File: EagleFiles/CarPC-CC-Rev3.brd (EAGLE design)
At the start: 75.5 x 80 mm, 72 parts, among them IC10 RN42HID-I/RM, IC2 MCP2515-I_SO, IC3 TJA1050T-CM/118, IC4 INA219AIDR, K1 G3VM-61VR(TR), Q5 16MHz

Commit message: Error in schemic and board: using 5v rail now
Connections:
- net +3V3-ODROID: now also JP-N2.2; no longer JP-N2.1
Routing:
- net +3V3-ODROID: track 3.36 -> 4.34 mm
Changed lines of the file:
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@@
 <drawing>
 <settings>
-<setting alwaysvectorfont="yes"/>
+<setting alwaysvectorfont="no"/>
 <setting verticaltext="up"/>
 </settings>
@@
 </layers>
 <board>
-<fusionsync huburn="a.YnVzaW5lc3M6Z29vZ2xlbWFpbDM5NzQ" projecturn="a.YnVzaW5lc3M6Z29vZ2xlbWFpbDM5NzQjRDIwMjAwMjA2MjYyODQ5OTA2" f3durn="urn:adsk.wipprod:dm.lineage:IggFrhZtQ_a1feRvvqs7Pg" pcbguid="bf3eb248-23ff-493d-88a3-1bcde9847c90" lastpulledtime="" lastsyncedchangeguid="898adb16-6d4d-edbb-685e-6e754855c02e"/>
+<fusionsync huburn="a.YnVzaW5lc3M6Z29vZ2xlbWFpbDM5NzQ" projecturn="a.YnVzaW5lc3M6Z29vZ2xlbWFpbDM5NzQjRDIwMjAwMjA2MjYyODQ5OTA2" f3durn="urn:adsk.wipprod:dm.lineage:80bHzjXET0ueI-K0PMmWLg" pcbguid="6e002f67-a89e-4d15-bfc3-ee707e087338" lastpulledtime="" lastsyncedchangeguid="95f337ff-36ca-174e-4e19-b75f39ef2b8f"/>
 <fusionteam huburn="a.YnVzaW5lc3M6Z29vZ2xlbWFpbDM5NzQ" projecturn="a.YnVzaW5lc3M6Z29vZ2xlbWFpbDM5NzQjRDIwMjAwMjA2MjYyODQ5OTA2" folderUrn="urn:adsk.wipprod:fs.folder:co.GUaS0R9CR3qfWpvkudDapg" urn="urn:adsk.wipprod:dm.lineage:FOIr01fbTJunwoKxbafz_w"  versionUrn="urn:adsk.wipprod:fs.file:vf.FOIr01fbTJunwoKxbafz_w?version=3" camFileUrn="" camFileVersionUrn="" lastpublishedchangeguid="8b2acdfd-6c5f-7b93-8b8e-7720c5fae449"/>
 <plain>
@@
 <signal name="+3V3-ODROID">
 <contactref element="R1" pad="1"/>
-<contactref element="JP-N2" pad="1"/>
-<wire x1="61.75" y1="96.75" x2="64.75" y2="96.75" width="0.5" layer="16"/>
 <wire x1="64.75" y1="96.75" x2="64.77" y2="96.672" width="0.5" layer="16"/>
-<wire x1="61.75" y1="96.75" x2="61.595" y2="96.52" width="0.5" layer="16"/>
+<contactref element="JP-N2" pad="2"/>
+<wire x1="62" y1="94" x2="64.5" y2="96.5" width="0.5" layer="16"/>
+<wire x1="64.5" y1="96.5" x2="64.77" y2="96.672" width="0.5" layer="16"/>
+<wire x1="62" y1="94" x2="61.595" y2="93.98" width="0.5" layer="16"/>
 </signal>
 <signal name="ODROID-PWR-SENS" class="7">

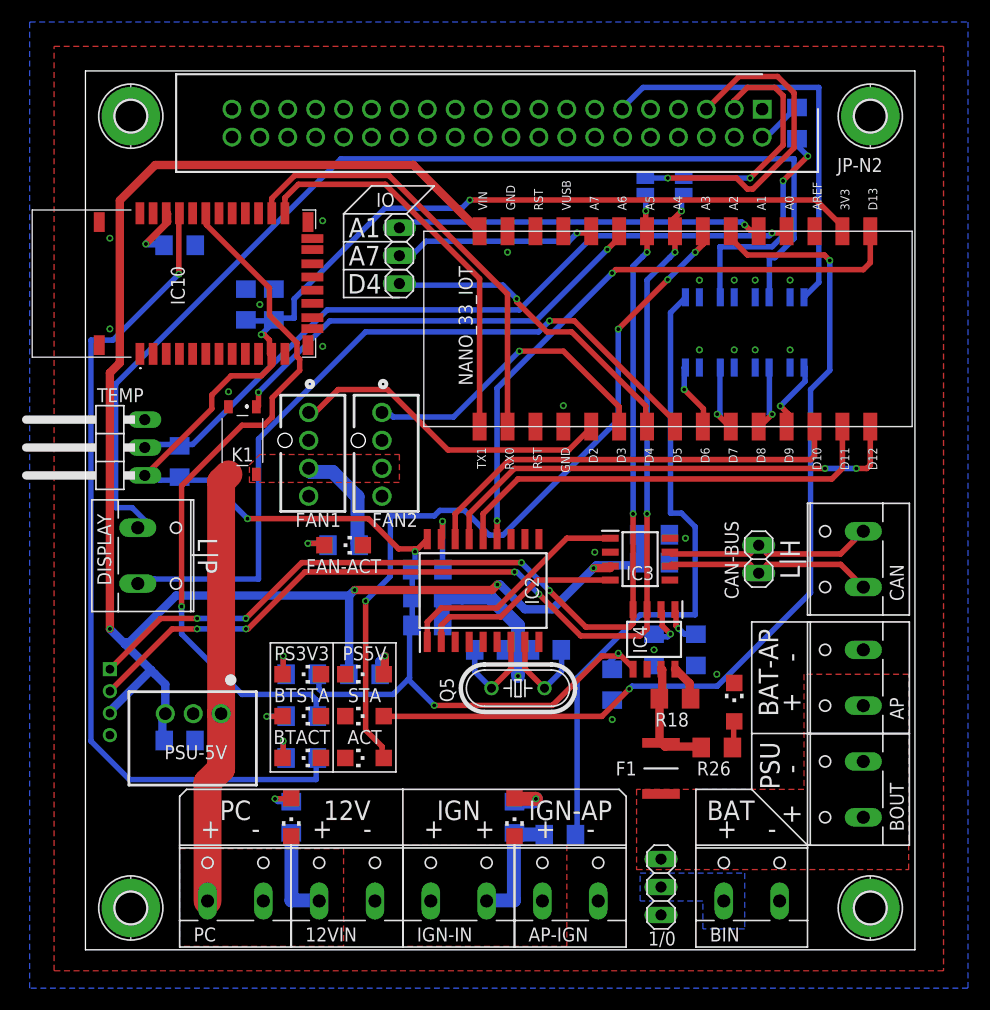
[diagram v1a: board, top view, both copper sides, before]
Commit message: Fan control interferes with display brightness.
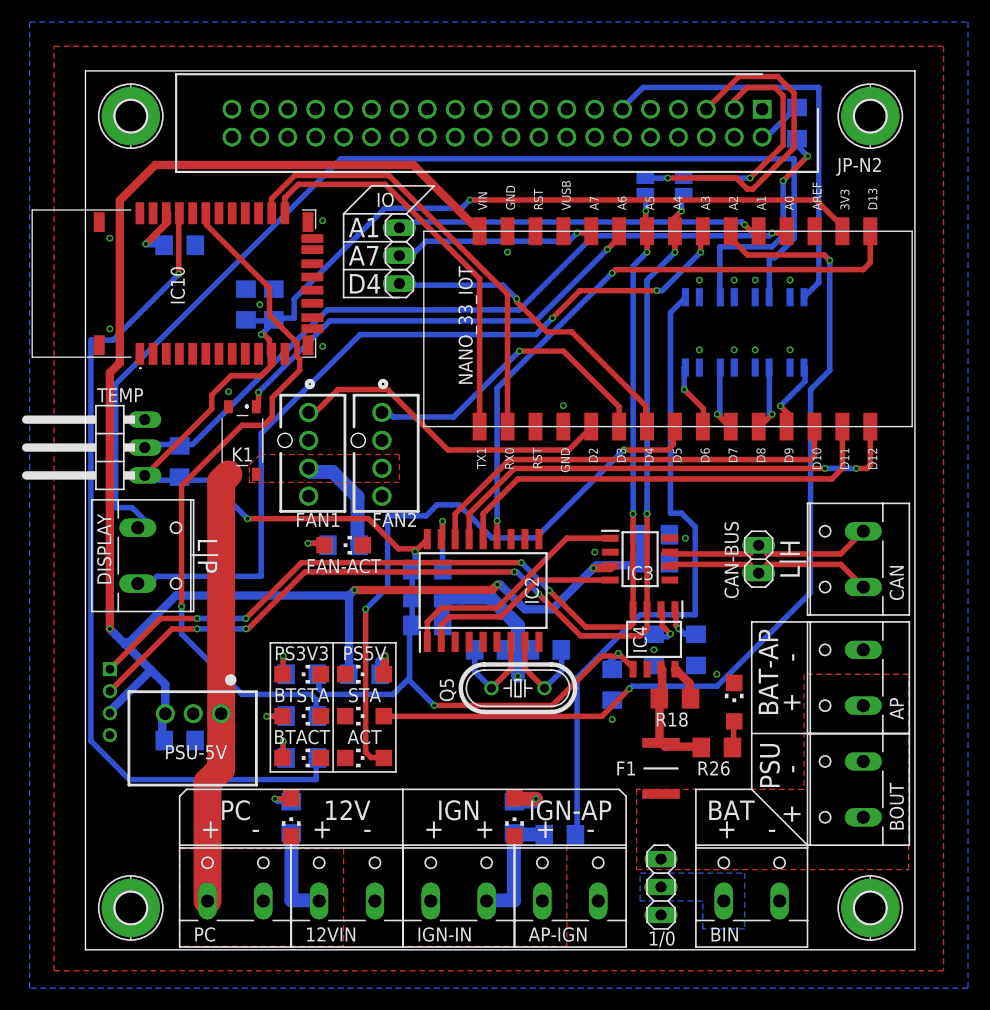
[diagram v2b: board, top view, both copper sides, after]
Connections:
- net DISP-BRIGHT: now also NANO_33_IOT.A3; no longer NANO_33_IOT.D5
- net LED-ACT: now also NANO_33_IOT.D5; no longer NANO_33_IOT.A3
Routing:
- net LED-ACT: track 70.3 -> 57.1 mm, vias 4 -> 2
- net DISP-BRIGHT: track 70.5 -> 73.3 mm, vias 1 -> 3
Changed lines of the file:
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@@
 </signal>
 <signal name="DISP-BRIGHT" class="7">
-<contactref element="NANO_33_IOT" pad="D5"/>
 <contactref element="DISPLAY" pad="2"/>
-<wire x1="53.5" y1="68.25" x2="53.5" y2="67.75" width="0.5" layer="1"/>
-<wire x1="44.5" y1="77.25" x2="53.5" y2="68.25" width="0.5" layer="1"/>
-<wire x1="42.25" y1="77.25" x2="44.5" y2="77.25" width="0.5" layer="1"/>
-<wire x1="41.25" y1="76.25" x2="42.25" y2="77.25" width="0.5" layer="16"/>
-<wire x1="25.5" y1="76.25" x2="41.25" y2="76.25" width="0.5" layer="16"/>
-<wire x1="15.75" y1="66.5" x2="25.5" y2="76.25" width="0.5" layer="16"/>
-<wire x1="15.75" y1="53.75" x2="15.75" y2="66.5" width="0.5" layer="16"/>
-<wire x1="6.25" y1="53.75" x2="15.75" y2="53.75" width="0.5" layer="16"/>
-<wire x1="6" y1="53.5" x2="6.25" y2="53.75" width="0.5" layer="16"/>
+<contactref element="NANO_33_IOT" pad="A3"/>
+<wire x1="56" y1="83.5" x2="56" y2="85" width="0.5" layer="1"/>
+<wire x1="52.5" y1="80" x2="56" y2="83.5" width="0.5" layer="16"/>
+<wire x1="52" y1="80" x2="52.5" y2="80" width="0.5" layer="16"/>
+<wire x1="45" y1="80" x2="52" y2="80" width="0.5" layer="1"/>
+<wire x1="42.5" y1="77.5" x2="45" y2="80" width="0.5" layer="1"/>
+<wire x1="41" y1="76" x2="42.5" y2="77.5" width="0.5" layer="16"/>
+<wire x1="25" y1="76" x2="41" y2="76" width="0.5" layer="16"/>
+<wire x1="16" y1="67" x2="25" y2="76" width="0.5" layer="16"/>
+<wire x1="16" y1="54" x2="16" y2="67" width="0.5" layer="16"/>
+<wire x1="6.5" y1="54" x2="16" y2="54" width="0.5" layer="16"/>
+<wire x1="6" y1="53.5" x2="6.5" y2="54" width="0.5" layer="16"/>
 <wire x1="5" y1="53.5" x2="6" y2="53.5" width="0.5" layer="16"/>
-<wire x1="53.5" y1="67.75" x2="53.6575" y2="67.6275" width="0.5" layer="1"/>
+<wire x1="56" y1="85" x2="56.1975" y2="85.4075" width="0.5" layer="1"/>
 <wire x1="5" y1="53.5" x2="4.7625" y2="53.34" width="0.5" layer="16"/>
-<via x="42.25" y="77.25" extent="1-16" drill="0.35"/>
+<via x="56" y="83.5" extent="1-16" drill="0.35"/>
+<via x="52" y="80" extent="1-16" drill="0.35"/>
+<via x="42.5" y="77.5" extent="1-16" drill="0.35"/>
 </signal>
 <signal name="+3V3" class="7">
@@
 </signal>
 <signal name="LED-ACT">
-<contactref element="NANO_33_IOT" pad="A3"/>
 <contactref element="ACT" pad="A"/>
-<wire x1="27" y1="38.5" x2="27" y2="37.5" width="0.5" layer="1"/>
-<wire x1="25.5" y1="40" x2="27" y2="38.5" width="0.5" layer="1"/>
-<wire x1="25.5" y1="51.75" x2="25.5" y2="40" width="0.5" layer="1"/>
-<wire x1="27.75" y1="54" x2="25.5" y2="51.75" width="0.5" layer="16"/>
-<wire x1="27.75" y1="59.5" x2="27.75" y2="54" width="0.5" layer="16"/>
-<wire x1="31.75" y1="59.5" x2="27.75" y2="59.5" width="0.5" layer="16"/>
-<wire x1="32.25" y1="60" x2="31.75" y2="59.5" width="0.5" layer="16"/>
-<wire x1="34.5" y1="60" x2="32.25" y2="60" width="0.5" layer="16"/>
-<wire x1="36.75" y1="57.75" x2="34.5" y2="60" width="0.5" layer="16"/>
-<wire x1="38" y1="57.75" x2="36.75" y2="57.75" width="0.5" layer="16"/>
-<wire x1="48.5" y1="68.25" x2="38" y2="57.75" width="0.5" layer="16"/>
-<wire x1="48.5" y1="76.5" x2="48.5" y2="68.25" width="0.5" layer="16"/>
-<wire x1="53" y1="81" x2="48.5" y2="76.5" width="0.5" layer="1"/>
-<wire x1="55.5" y1="83.5" x2="53" y2="81" width="0.5" layer="16"/>
-<wire x1="56.25" y1="84.25" x2="55.5" y2="83.5" width="0.5" layer="1"/>
-<wire x1="56.25" y1="85.25" x2="56.25" y2="84.25" width="0.5" layer="1"/>
+<contactref element="NANO_33_IOT" pad="D5"/>
+<wire x1="26" y1="37.5" x2="27" y2="37.5" width="0.5" layer="1"/>
+<wire x1="25.5" y1="38" x2="26" y2="37.5" width="0.5" layer="1"/>
+<wire x1="25.5" y1="51" x2="25.5" y2="38" width="0.5" layer="1"/>
+<wire x1="27.5" y1="53" x2="25.5" y2="51" width="0.5" layer="16"/>
+<wire x1="27.5" y1="59.5" x2="27.5" y2="53" width="0.5" layer="16"/>
+<wire x1="31" y1="59.5" x2="27.5" y2="59.5" width="0.5" layer="16"/>
+<wire x1="32" y1="60.5" x2="31" y2="59.5" width="0.5" layer="16"/>
+<wire x1="34" y1="60.5" x2="32" y2="60.5" width="0.5" layer="16"/>
+<wire x1="37" y1="57.5" x2="34" y2="60.5" width="0.5" layer="16"/>
+<wire x1="41" y1="57.5" x2="37" y2="57.5" width="0.5" layer="16"/>
+<wire x1="49" y1="65.5" x2="41" y2="57.5" width="0.5" layer="16"/>
+<wire x1="53" y1="65.5" x2="49" y2="65.5" width="0.5" layer="1"/>
+<wire x1="53.5" y1="66" x2="53" y2="65.5" width="0.5" layer="1"/>
+<wire x1="53.5" y1="67.5" x2="53.5" y2="66" width="0.5" layer="1"/>
 <wire x1="27" y1="37.5" x2="27.15" y2="37.465" width="0.5" layer="1"/>
-<wire x1="56.25" y1="85.25" x2="56.1975" y2="85.4075" width="0.5" layer="1"/>
-<via x="25.5" y="51.75" extent="1-16" drill="0.35"/>
-<via x="48.5" y="76.5" extent="1-16" drill="0.35"/>
-<via x="53" y="81" extent="1-16" drill="0.35"/>
-<via x="55.5" y="83.5" extent="1-16" drill="0.35"/>
+<wire x1="53.5" y1="67.5" x2="53.6575" y2="67.6275" width="0.5" layer="1"/>
+<via x="25.5" y="51" extent="1-16" drill="0.35"/>
+<via x="49" y="65.5" extent="1-16" drill="0.35"/>
 </signal>
 <signal name="BT-TX0">
